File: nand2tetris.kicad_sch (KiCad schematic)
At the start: 9 parts

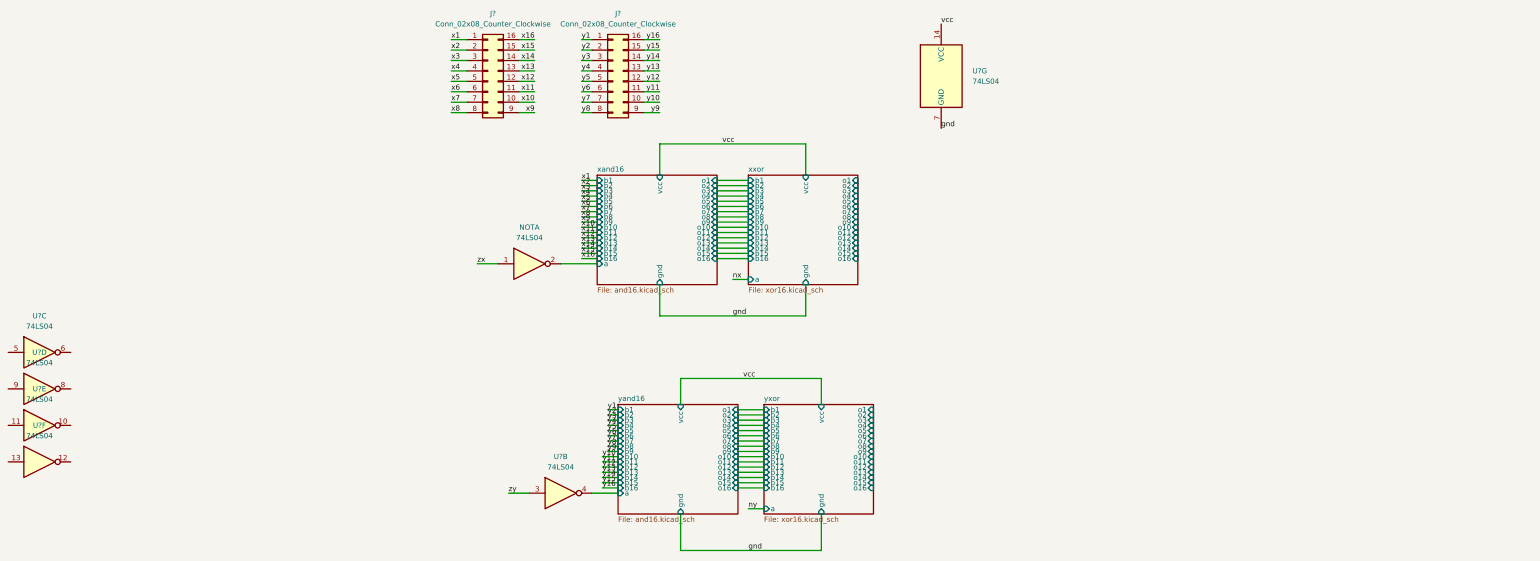
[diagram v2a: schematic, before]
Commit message: Finish schematic
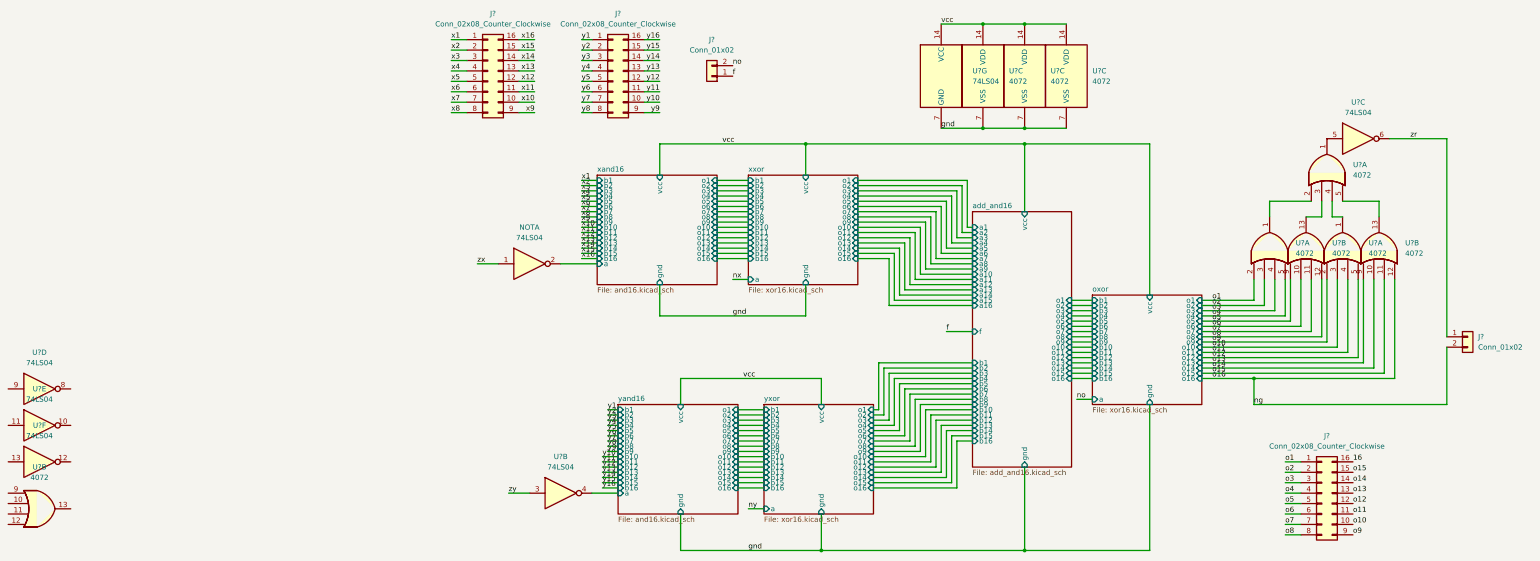
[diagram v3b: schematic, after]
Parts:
- added J?: Conn_02x08_Counter_Clockwise, symbol Connector_Generic:Conn_02x08_Counter_Clockwise
- added J? (x2): Conn_01x02, symbol Connector_Generic:Conn_01x02
- added U? (x9): 4072, symbol 4xxx:4072
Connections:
- net gnd: now also U?.7 (VSS), U?.7 (VSS), U?.7 (VSS)
- net vcc: now also U?.14 (VDD), U?.14 (VDD), U?.14 (VDD)
- net at U?.5: now also U?.1
- net zr: now reaches U?.6
- net zr: now also J?.1 (Pin_1)
- new net: U?.1, U?.2
- new net: U?.13, U?.3
- new net: U?.1, U?.4
- new net: U?.13, U?.5
- new net 16: J?.16 (Pin_16)
- new net f: J?.1 (Pin_1)
- new net ng: J?.2 (Pin_2), U?.12
- new net no: J?.2 (Pin_2)
- new net o1: J?.1 (Pin_1), U?.2
- new net o10: J?.10 (Pin_10), U?.3
- new net o11: J?.11 (Pin_11), U?.4
- new net o12: J?.12 (Pin_12), U?.5
- new net o13: J?.13 (Pin_13), U?.9
- new net o14: J?.14 (Pin_14), U?.10
- new net o15: J?.15 (Pin_15), U?.11
- new net o2: J?.2 (Pin_2), U?.3
- new net o3: J?.3 (Pin_3), U?.4
- new net o4: J?.4 (Pin_4), U?.5
- new net o5: J?.5 (Pin_5), U?.9
- new net o6: J?.6 (Pin_6), U?.10
- new net o7: J?.7 (Pin_7), U?.11
- new net o8: J?.8 (Pin_8), U?.12
- new net o9: J?.9 (Pin_9), U?.2
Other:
- added sheet add_and16 (add_and16.kicad_sch)
- added sheet oxor (xor16.kicad_sch)
- moved on the sheet: U?C
